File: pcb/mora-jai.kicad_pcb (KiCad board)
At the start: 2 copper layers, 150 x 150 mm, 68 parts, among them J1 Conn_01x02, J2 Conn_01x04, SW1 SW_Push, SW10 SW_Push, SW11 SW_Push, SW12 SW_Push, SW13 SW_Push, SW14 SW_Push, SW15 SW_Push, SW16 SW_Push, SW2 SW_Push, SW3 SW_Push, SW4 SW_Push, SW5 SW_Push, SW6 SW_Push, SW7 SW_Push, SW8 SW_Push, SW9 SW_Push, U1 CD74HC4067M, U3 XIAO-ESP32-S3-SMD

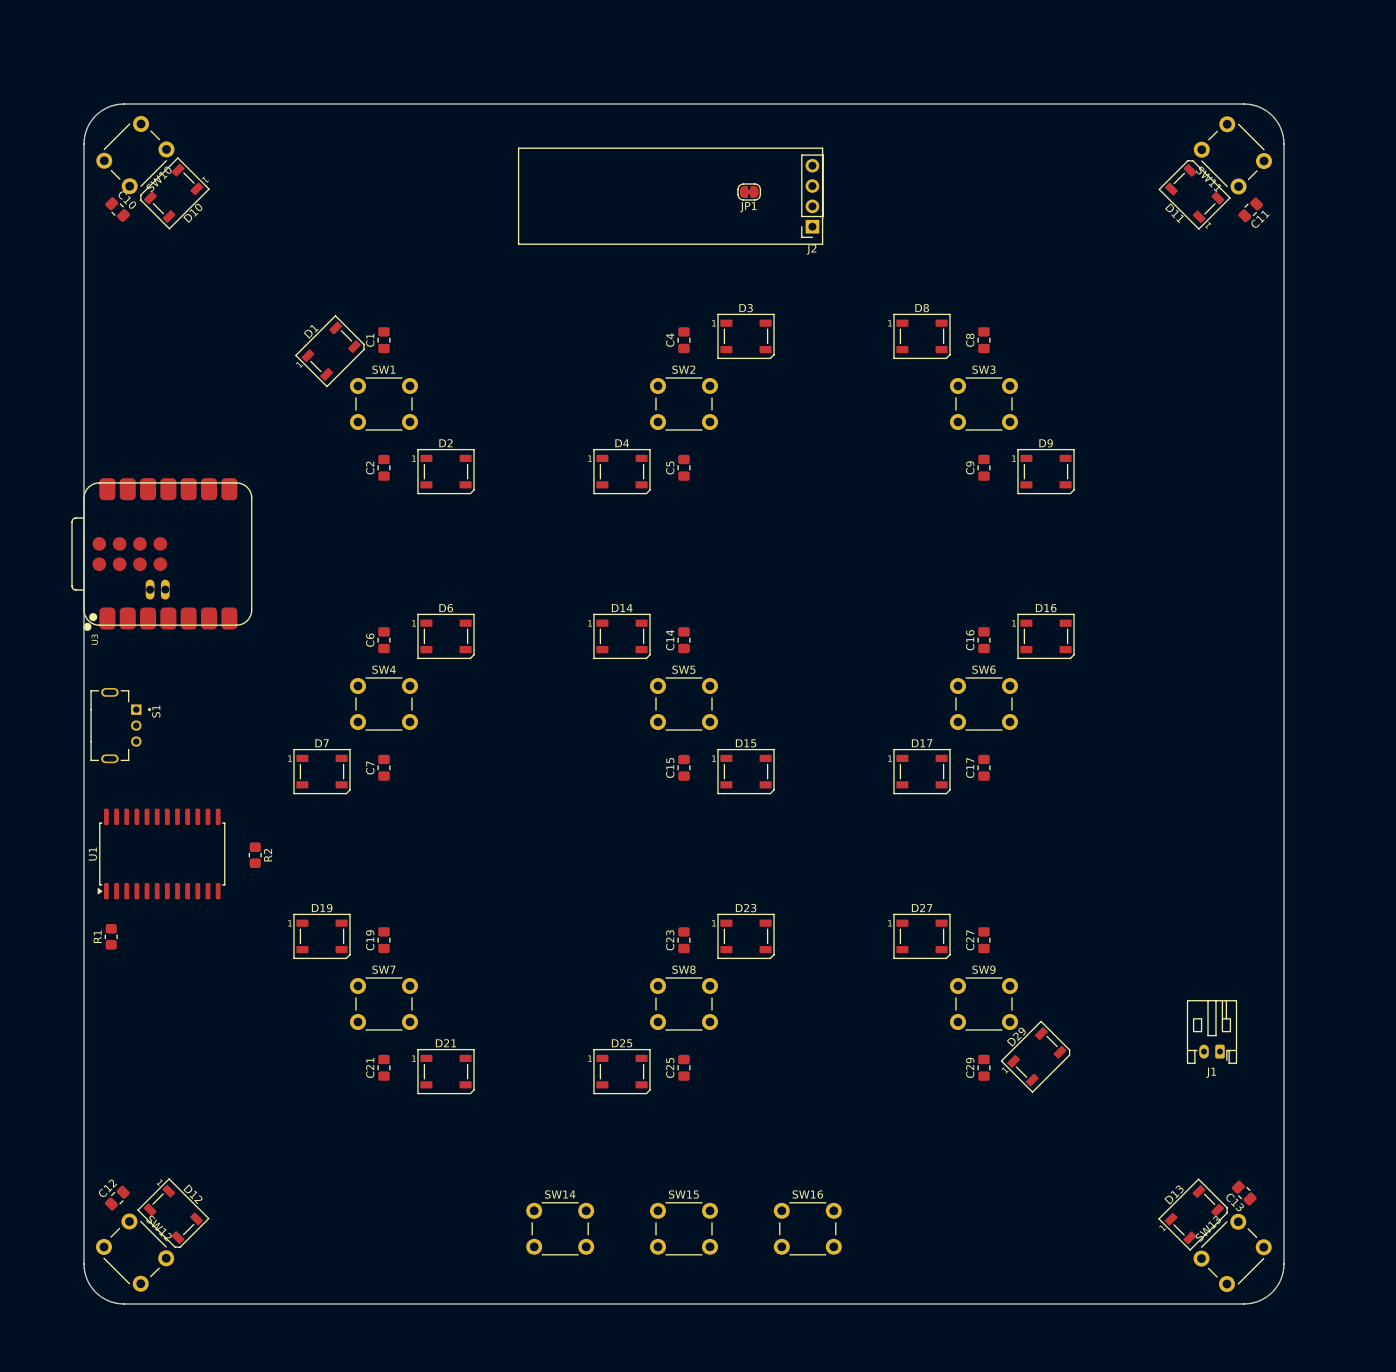
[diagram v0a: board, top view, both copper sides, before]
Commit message: begin routing LED matrix, repositioned more components
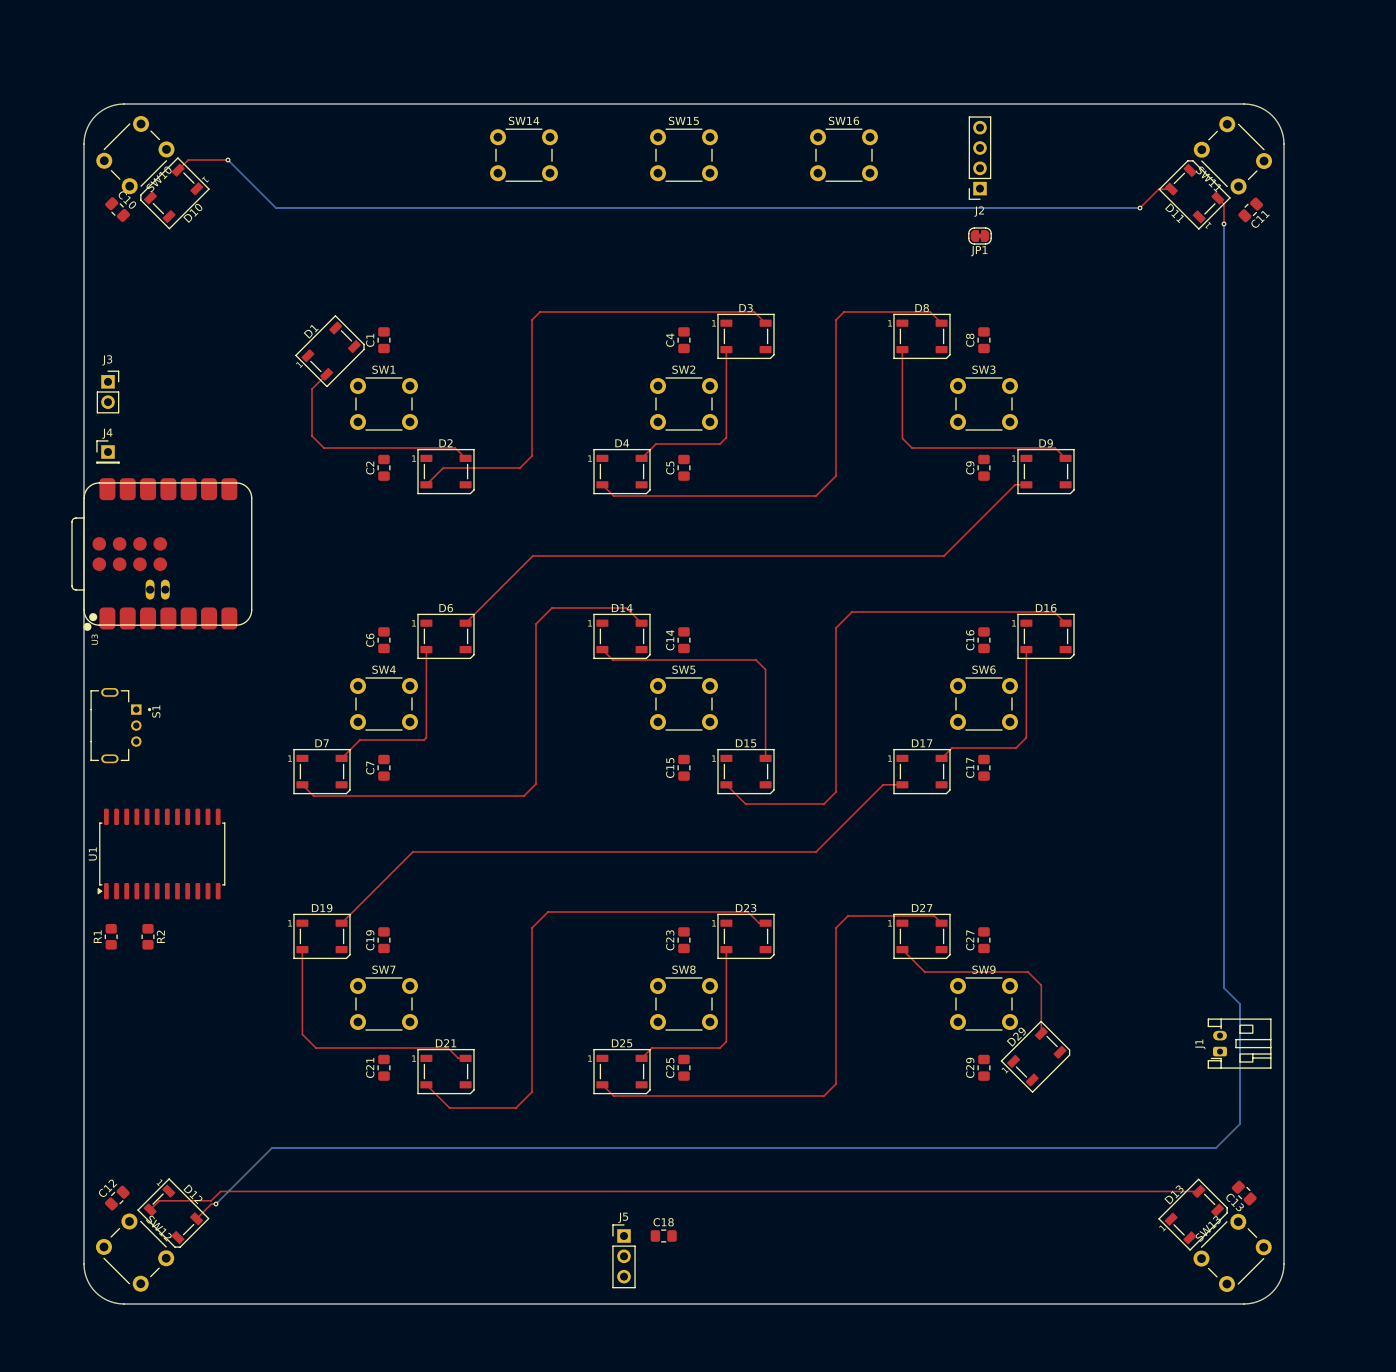
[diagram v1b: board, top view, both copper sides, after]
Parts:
- added C18: 100 uF, Capacitor_SMD:C_0805_2012Metric_Pad1.18x1.45mm_HandSolder, F.Cu at (98.5, 164.5)
- added J3: Conn_01x02, Connector_PinSocket_2.54mm:PinSocket_1x02_P2.54mm_Vertical, F.Cu at (29.0, 57.7)
- added J4: Conn_01x01, Connector_PinHeader_2.54mm:PinHeader_1x01_P2.54mm_Vertical, F.Cu at (29.0, 66.5)
- added J5: Conn_01x03, Connector_PinHeader_2.54mm:PinHeader_1x03_P2.54mm_Vertical, F.Cu at (93.5, 164.5)
- moved SW14 134.3 mm to (77.8, 27.1)
- moved SW16 134.3 mm to (117.8, 27.1)
- moved SW15 134.2 mm to (97.8, 27.1)
- moved JP1 29.4 mm to (138.0, 39.5)
- moved J2 21.5 mm to (138.0, 33.6)
- moved R2 16.8 mm to (34.0, 127.1)
- turned J1 to 90 degrees
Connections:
- U3 pad 10: unconnected-(U3-GPIO8_A9_D9_MISO-Pad10) -> MTR_CTRL
- U3 pad 9: unconnected-(U3-GPIO7_A8_D8_SCK-Pad9) -> D8_PIN
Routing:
- net Net-(D11-DOUT): track 0.00 -> 252.2 mm, vias 0 -> 2
- net Net-(D12-DOUT): track 0.00 -> 132.0 mm
- net Net-(D10-DOUT): track 0.00 -> 128.1 mm, vias 0 -> 2
- net Net-(D6-DIN): track 0.00 -> 77.3 mm
- net Net-(D17-DOUT): track 0.00 -> 77.3 mm
- net Net-(D21-DOUT): track 0.00 -> 66.3 mm
- net Net-(D15-DOUT): track 0.00 -> 65.9 mm
- net Net-(D14-DIN): track 0.00 -> 65.2 mm
- net Net-(D4-DOUT): track 0.00 -> 64.5 mm
- net Net-(D25-DOUT): track 0.00 -> 64.1 mm
- net Net-(D2-DOUT): track 0.00 -> 61.9 mm
- net Net-(D14-DOUT): track 0.00 -> 32.5 mm
- net Net-(D8-DOUT): track 0.00 -> 32.5 mm
- net Net-(D19-DOUT): track 0.00 -> 32.2 mm
- net Net-(D1-DOUT): track 0.00 -> 28.8 mm
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
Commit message: lots of routing
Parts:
- removed JP1: SolderJumper_2_Bridged, Jumper:SolderJumper-2_P1.3mm_Bridged_RoundedPad1.0x1.5mm
- added JP2: SolderJumper_3_Bridged12, Jumper:SolderJumper-3_P1.3mm_Bridged12_RoundedPad1.0x1.5mm, F.Cu at (133.0, 28.5)
- moved R1 23.8 mm to (46.0, 110.0), turned to -90 degrees
- moved R2 17.0 mm to (46.0, 115.0)
- turned U1 to -90 degrees
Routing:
- net +5V: track 0.00 -> 905.4 mm, vias 0 -> 22
- net Net-(D10-DIN): track 0.00 -> 230.4 mm
- net Net-(J1-Pin_1): track 0.00 -> 163.1 mm, vias 0 -> 1
- net +3V3: track 0.00 -> 135.5 mm, vias 0 -> 2
- net /MUX_EN: track 0.00 -> 63.0 mm
- net LED_DATA_IN: track 0.00 -> 31.1 mm
- net /MUX_OUT: track 0.00 -> 29.1 mm
- net +BATT: track 0.00 -> 19.8 mm, vias 0 -> 1
- net D8_PIN: track 0.00 -> 16.3 mm, vias 0 -> 1
- net Net-(D8-DOUT): track 32.5 -> 39.3 mm, vias 0 -> 2
- net /SW_9: track 0.00 -> 6.50 mm
- net /SW_11: track 0.00 -> 6.50 mm
- net /SW_10: track 0.00 -> 6.50 mm
- net /SW_12: track 0.00 -> 6.50 mm
- net /SW_8: track 0.00 -> 6.50 mm
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- added copper zone on B.Cu, net GND
- added copper zone on F.Cu, net GND

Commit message: reposition power switch, routing
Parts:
- moved J1 84.9 mm to (168.0, 56.5)
- moved S1 42.6 mm to (29.2, 58.1)
- moved R2 19.2 mm to (31.3, 127.4)
- moved R1 13.8 mm to (33.0, 105.5)
- moved J3 12.5 mm to (29.5, 45.2)
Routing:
- net /SW_10: track 6.50 -> 216.8 mm, vias 0 -> 6
- net Net-(J1-Pin_1): track 163.1 -> 0.00 mm, vias 1 -> 0
- net /SW_15: track 6.50 -> 168.5 mm, vias 0 -> 4
- net /SW_14: track 6.50 -> 149.7 mm, vias 0 -> 4
- net /SW_13: track 6.50 -> 130.2 mm, vias 0 -> 4
- net /SW_1: track 6.50 -> 95.7 mm, vias 0 -> 4
- net /SW_0: track 6.50 -> 75.7 mm, vias 0 -> 4
- net /CH_2: track 0.00 -> 39.7 mm, vias 0 -> 4
- net /CH_3: track 0.00 -> 39.3 mm, vias 0 -> 4
- net +3V3: track 135.5 -> 171.6 mm, vias 2 -> 4
- net +5V: track 905.4 -> 871.0 mm
- net /CH_0: track 0.00 -> 26.5 mm, vias 0 -> 2
- net /CH_1: track 0.00 -> 25.4 mm
- net +BATT: track 19.8 -> 32.1 mm, vias 1 -> 4
- net /MUX_OUT: track 29.1 -> 40.4 mm
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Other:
- board text added: "TODO: Import and check sketches: - buttonRailsSketch.dxf - BoxTopCutouts.dxf"
- board text added: "TODO: Reposition battery connector according to sketch"
